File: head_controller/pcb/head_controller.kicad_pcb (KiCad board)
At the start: 2 copper layers, 59.3 x 132.3 mm, 28 parts, among them P1 HEADER_02X08_SMD

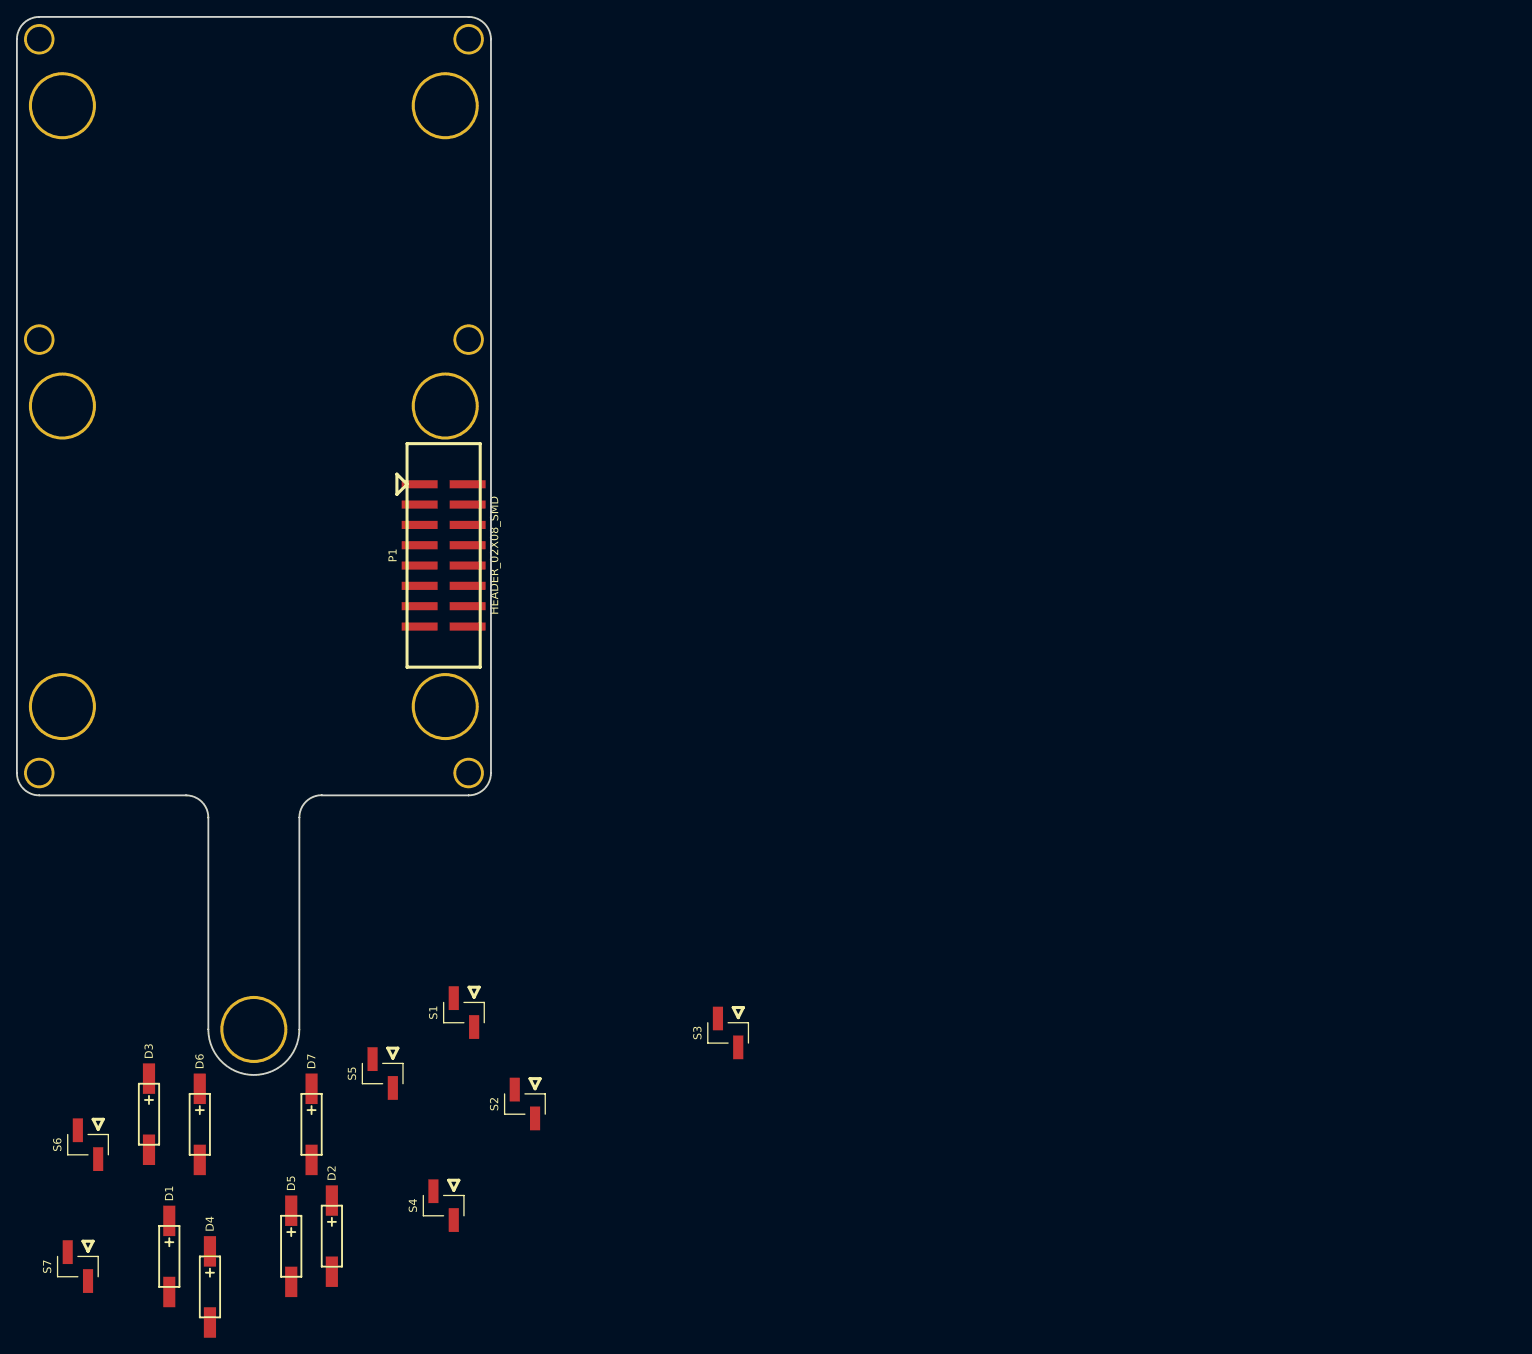
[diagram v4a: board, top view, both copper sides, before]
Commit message: Expanded board and added 8th valve and led.
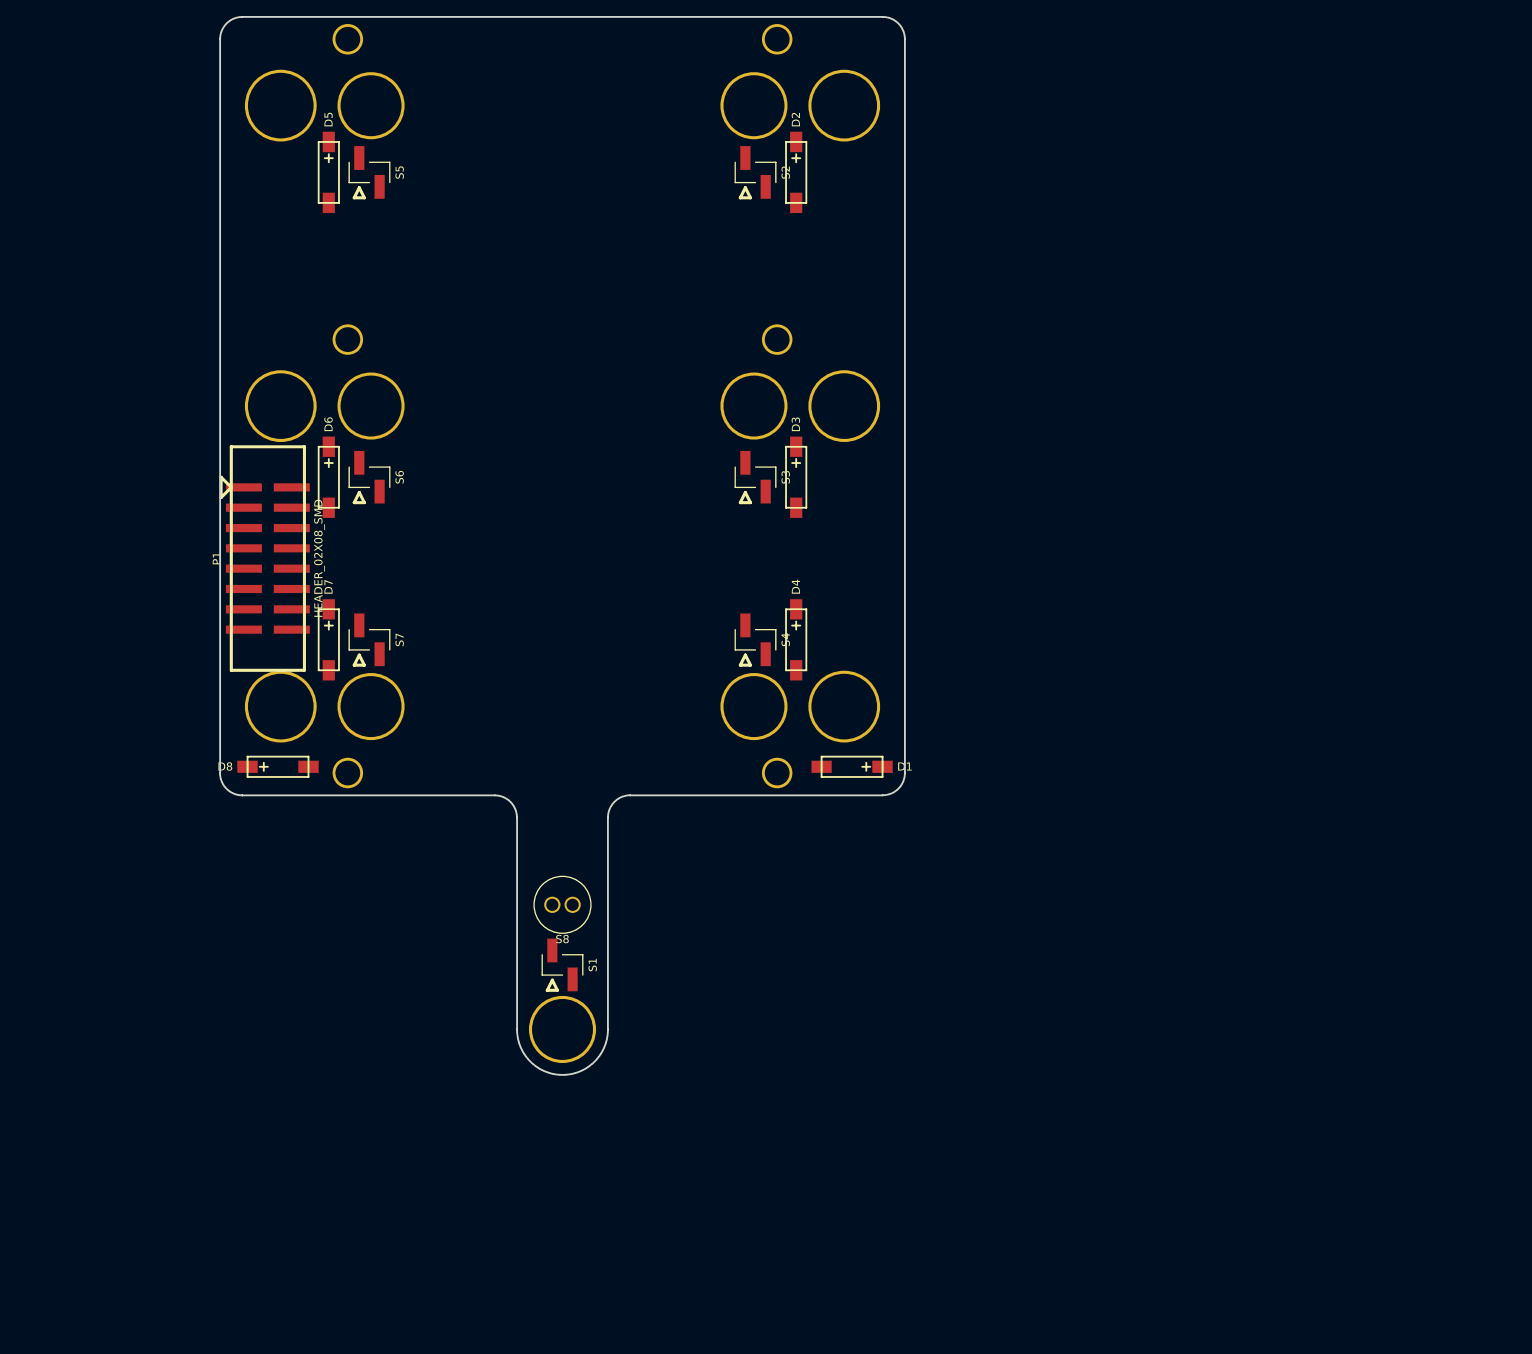
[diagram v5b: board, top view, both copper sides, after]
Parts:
- added D8: LED_24V_SMD, head_controller:LED_555-3XXX_SMD, F.Cu at (58.0, 119.1)
- added REF**: clearance_hole, head_controller:clearance_hole, F.Cu at (58.4, 36.5)
- added REF**: clearance_hole, head_controller:clearance_hole, F.Cu at (58.4, 74.1)
- added REF**: clearance_hole, head_controller:clearance_hole, F.Cu at (58.4, 111.6)
- added REF**: clearance_hole, head_controller:clearance_hole, F.Cu at (128.8, 36.5)
- added REF**: clearance_hole, head_controller:clearance_hole, F.Cu at (128.8, 74.1)
- added REF**: clearance_hole, head_controller:clearance_hole, F.Cu at (128.8, 111.6)
- added S8: LEE_VALVE_3WAY, head_controller:LEE_VALVE_PLUG_IN, F.Cu at (93.6, 136.4)
- moved D2 145.1 mm to (122.8, 44.8)
- moved D5 134.3 mm to (64.4, 44.8)
- moved S2 120.0 mm to (117.7, 44.8), turned to 180 degrees
- moved D3 113.5 mm to (122.8, 82.9)
- moved S5 112.7 mm to (69.5, 44.8), turned to 180 degrees
- moved D4 109.1 mm to (122.8, 103.3)
- moved D1 105.0 mm to (129.8, 119.1), turned to 270 degrees
- moved S6 90.5 mm to (69.5, 82.9), turned to 180 degrees
- moved S7 86.4 mm to (69.5, 103.3), turned to 180 degrees
- moved D6 82.5 mm to (64.4, 82.9)
- moved S4 80.8 mm to (117.7, 103.3), turned to 180 degrees
- moved S3 69.5 mm to (117.7, 82.9), turned to 180 degrees
- moved D7 60.6 mm to (64.4, 103.3)
- moved REF** 38.6 mm to (117.5, 74.0)
- moved REF** 38.6 mm to (117.5, 36.5)
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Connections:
- P1 pad 16: Net-(P1-Pad16) -> /OUT7
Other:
- board size 59.3 x 132.3 mm -> 85.6 x 132.3 mm

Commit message: Initial board layout.
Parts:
- added C1: 0.1uF, head_controller:SM1210, F.Cu at (96.1, 140.1)
- added C10: 0.1uF, head_controller:SM1210, F.Cu at (109.5, 111.5)
- added C11: 8.2nF, head_controller:SM1210, F.Cu at (102.5, 105.2)
- added C12: 0.1uF, head_controller:SM1210, F.Cu at (96.8, 98.2)
- added C13: 0.1uF, head_controller:SM1210, F.Cu at (77.7, 36.6)
- added C14: 8.2nF, head_controller:SM1210, F.Cu at (77.7, 49.3)
- added C15: 0.1uF, head_controller:SM1210, F.Cu at (71.4, 56.3)
- added C16: 0.1uF, head_controller:SM1210, F.Cu at (77.7, 74.1)
- added C17: 8.2nF, head_controller:SM1210, F.Cu at (77.7, 86.8)
- added C18: 0.1uF, head_controller:SM1210, F.Cu at (71.4, 93.7)
- added C19: 0.1uF, head_controller:SM1210, F.Cu at (77.7, 111.5)
- added C2: 8.2nF, head_controller:SM1210, F.Cu at (93.6, 122.9)
- added C20: 8.2nF, head_controller:SM1210, F.Cu at (84.7, 105.2)
- added C21: 0.1uF, head_controller:SM1210, F.Cu at (90.4, 98.2)
- added C3: 0.1uF, head_controller:SM1210, F.Cu at (87.2, 116.0)
- added C4: 0.1uF, head_controller:SM1210, F.Cu at (109.5, 36.6)
- added C5: 8.2nF, head_controller:SM1210, F.Cu at (109.5, 49.3)
- added C6: 0.1uF, head_controller:SM1210, F.Cu at (115.8, 56.3)
- added C7: 0.1uF, head_controller:SM1210, F.Cu at (109.5, 74.1)
- added C8: 8.2nF, head_controller:SM1210, F.Cu at (109.5, 86.8)
- added C9: 0.1uF, head_controller:SM1210, F.Cu at (115.8, 93.7)
- added P2: HEADER_02X05_SMD, head_controller:HEADER_02x05_SMD, F.Cu at (58.0, 55.0)
- added R1: 200k, head_controller:SM1210, F.Cu at (93.6, 129.3)
- added R2: 200k, head_controller:SM1210, F.Cu at (109.5, 42.9)
- added R3: 200k, head_controller:SM1210, F.Cu at (109.5, 80.4)
- added R4: 200k, head_controller:SM1210, F.Cu at (102.5, 111.5)
- added R5: 200k, head_controller:SM1210, F.Cu at (77.7, 42.9)
- added R6: 200k, head_controller:SM1210, F.Cu at (77.7, 80.4)
- added R7: 200k, head_controller:SM1210, F.Cu at (84.7, 111.5)
- added U1: HALL_DRV5053, head_controller:SOT-23-3, B.Cu at (93.6, 145.0)
- added U10: MAX4215, head_controller:SOIC_8_N, F.Cu at (77.7, 56.3)
- added U11: HALL_DRV5053, head_controller:SOT-23-3, B.Cu at (76.7, 74.1)
- added U12: MAX4215, head_controller:SOIC_8_N, F.Cu at (77.7, 93.7)
- added U13: HALL_DRV5053, head_controller:SOT-23-3, B.Cu at (76.7, 111.6)
- added U14: MAX4215, head_controller:SOIC_8_N, F.Cu at (84.7, 98.2)
- added U2: MAX4215, head_controller:SOIC_8_N, F.Cu at (93.6, 116.0)
- added U3: HALL_DRV5053, head_controller:SOT-23-3, B.Cu at (110.5, 36.5)
- added U4: MAX4215, head_controller:SOIC_8_N, F.Cu at (109.5, 56.3)
- added U5: HALL_DRV5053, head_controller:SOT-23-3, B.Cu at (110.5, 74.1)
- added U6: MAX4215, head_controller:SOIC_8_N, F.Cu at (109.5, 93.7)
- added U7: HALL_DRV5053, head_controller:SOT-23-3, B.Cu at (110.5, 111.6)
- added U8: MAX4215, head_controller:SOIC_8_N, F.Cu at (102.5, 98.2)
- added U9: HALL_DRV5053, head_controller:SOT-23-3, B.Cu at (76.7, 36.5)
- S8: value LEE_VALVE_3WAY -> LEE_VALVE_PLUG_IN
- moved D3 8.90 mm to (123.2, 74.1)
- moved D6 8.90 mm to (64.0, 74.1)
- moved D2 8.36 mm to (123.2, 36.5)
- moved D4 8.36 mm to (123.2, 111.6)
- moved D5 8.36 mm to (64.0, 36.5)
- moved D7 8.36 mm to (64.0, 111.6)
- moved P1 1.27 mm to (58.0, 93.1)
- moved D8 0.90 mm to (57.4, 118.5)
- moved D1 0.64 mm to (129.8, 118.5)
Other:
- board text added: "0"
- board text added: "1"
- board text added: "2"
- board text added: "3"
- board text added: "4"
- board text added: "5"
- board text added: "6"
- board text added: "7"

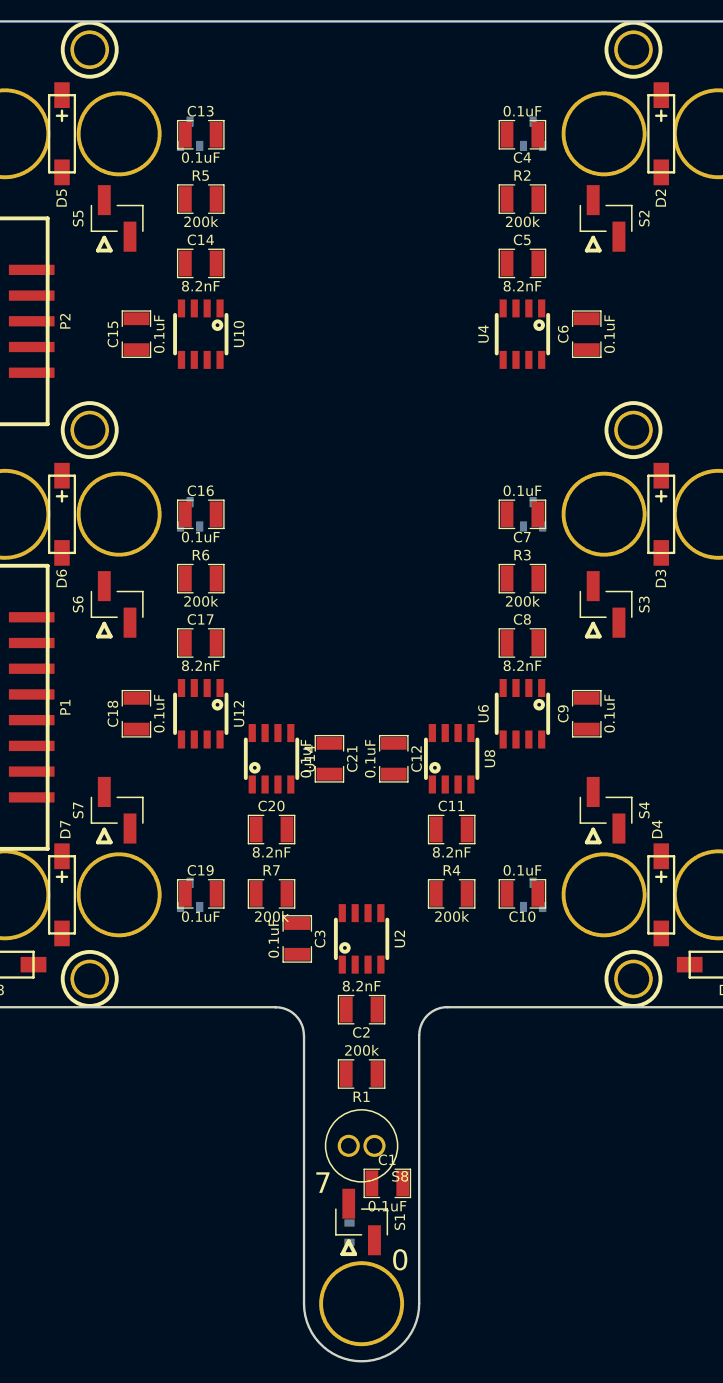
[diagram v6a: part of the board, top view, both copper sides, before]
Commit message: Moved some components.
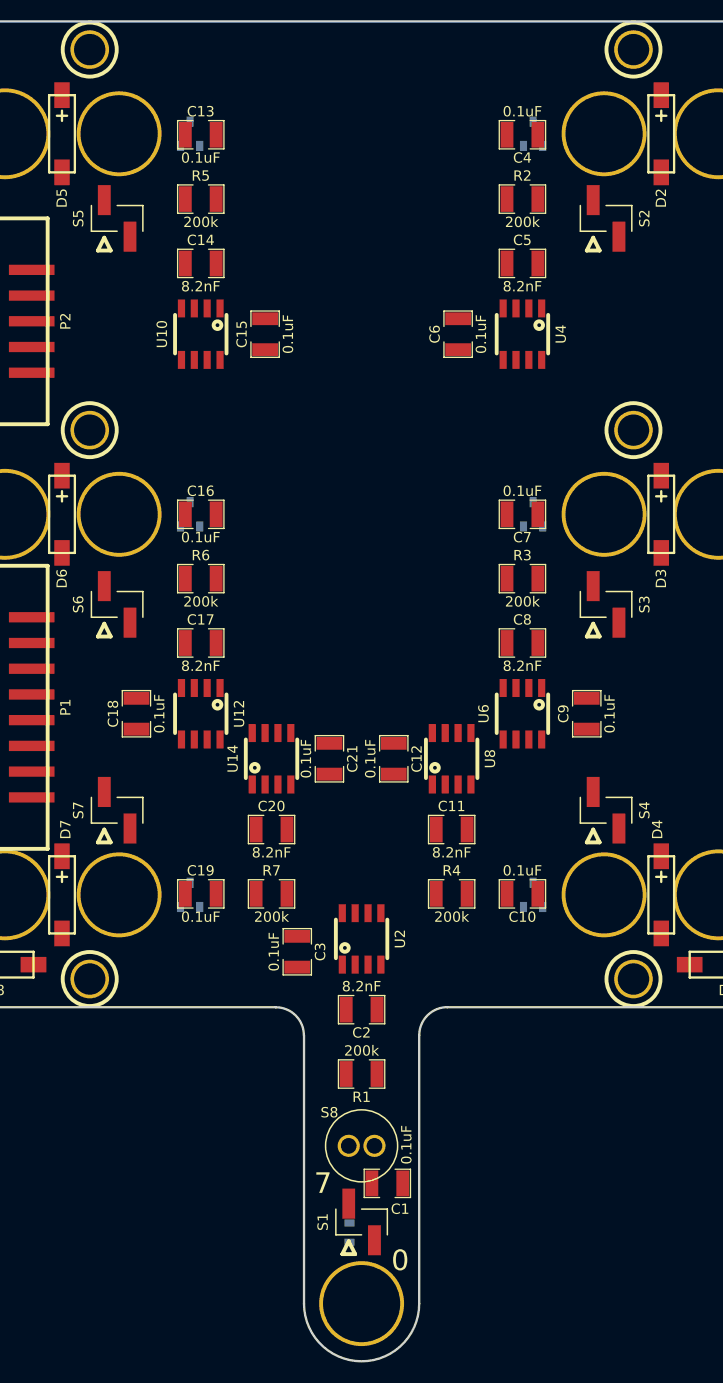
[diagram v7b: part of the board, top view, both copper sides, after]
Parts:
- moved C15 12.7 mm to (84.1, 56.3)
- moved C6 12.7 mm to (103.1, 56.3)
- moved C3 1.27 mm to (87.2, 117.2)
- renumbered REF** to CLEARANCE_HOLE_1, REF** to CLEARANCE_HOLE_2, REF** to CLEARANCE_HOLE_3, REF** to CLEARANCE_HOLE_4, REF** to CLEARANCE_HOLE_5, REF** to CLEARANCE_HOLE_6, REF** to MOUNTING_HOLE_1, REF** to MOUNTING_HOLE_2, REF** to MOUNTING_HOLE_3, REF** to MOUNTING_HOLE_4, REF** to MOUNTING_HOLE_5, REF** to MOUNTING_HOLE_6, REF** to VALVE_HOLE_1, REF** to VALVE_HOLE_2, REF** to VALVE_HOLE_3, REF** to VALVE_HOLE_4, REF** to VALVE_HOLE_5, REF** to VALVE_HOLE_6
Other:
- net class Default: clearance 0.2 -> 0.254; trace_width 0.25 -> 0.254; via_dia 0.6 -> 0.889; via_drill 0.4 -> 0.635
- net class GND added: clearance 0.254, trace_width 0.508, via_dia 0.889, via_drill 0.635
- net class POWER added: clearance 0.254, trace_width 0.8128, via_dia 0.889, via_drill 0.635
- net class SIGNAL added: clearance 0.254, trace_width 0.4064, via_dia 0.889, via_drill 0.635
- rule trace_clearance: 0.2 -> 0.254
